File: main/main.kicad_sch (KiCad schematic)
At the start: 37 parts, among them J3 USB_C_Receptacle_USB2.0_16P, J4 SM03B-SRSS-TB, Q1 DMG1012T-7, SW1 PTS810 SJK 250 SMTR LFS, U2 IC_ESPIF_ESP32-C3-MINI-1-N4, U3 W25Q32RVXHJQ TR, U5 450mA 4.2V, Y1 ECS-120-8-33-JGN-TR

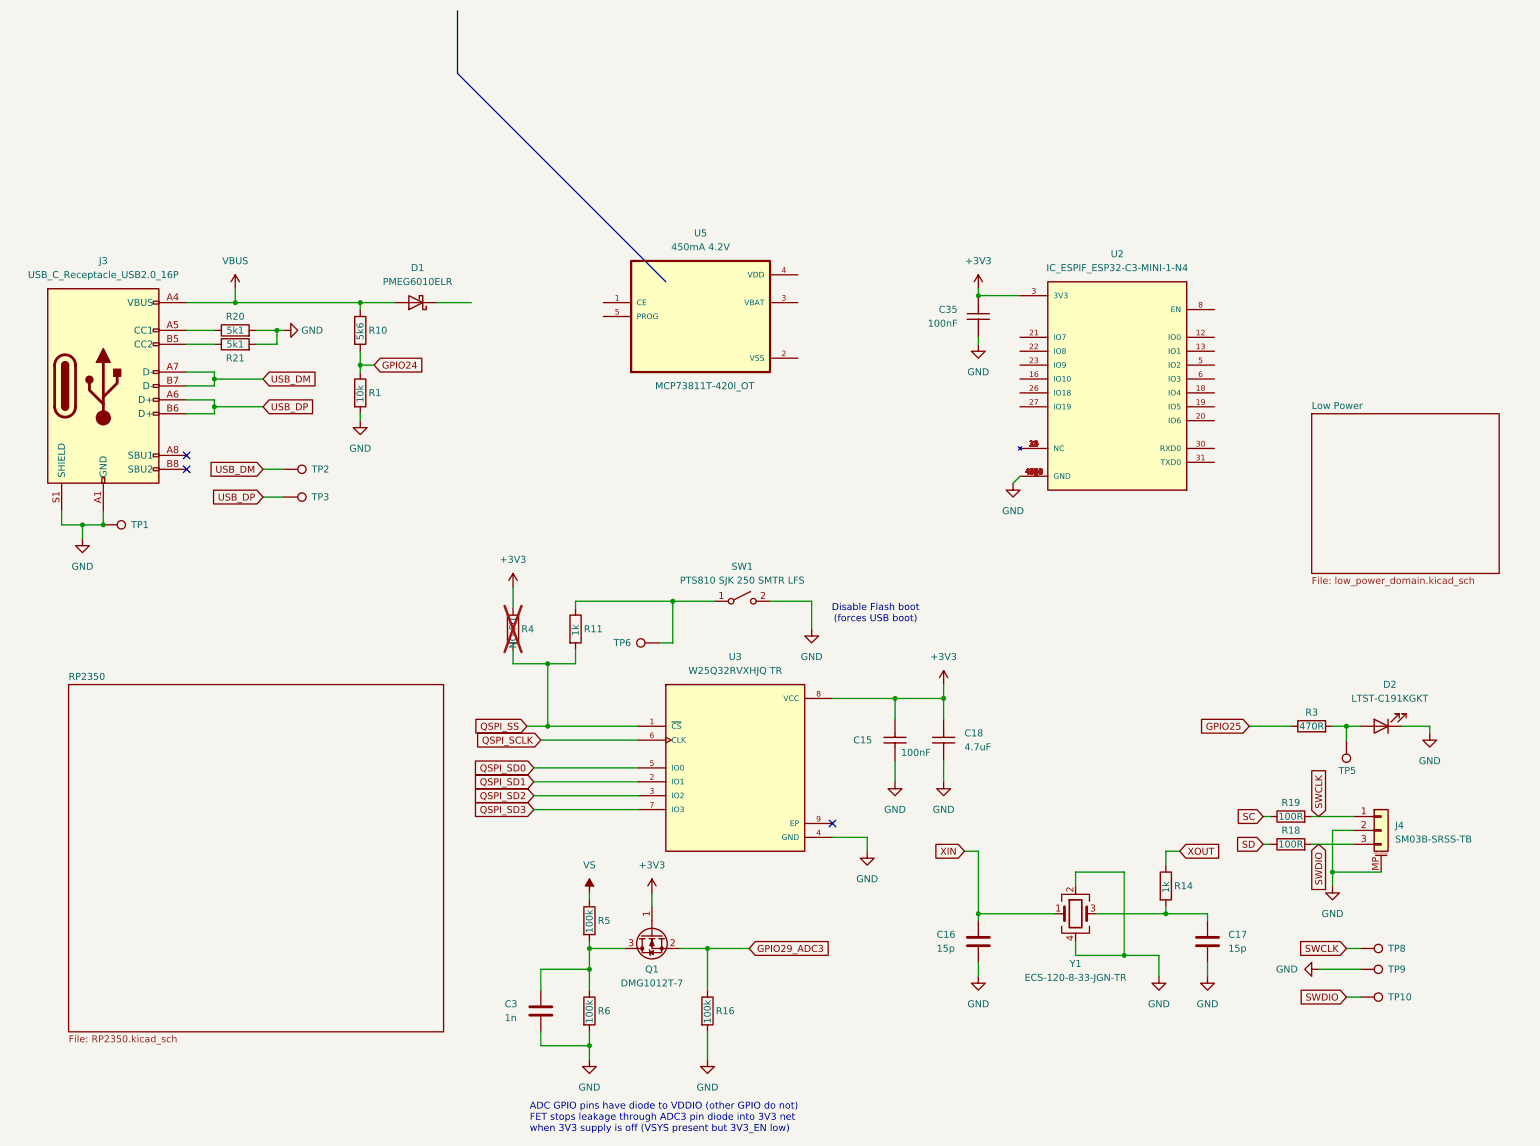
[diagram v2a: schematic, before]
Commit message: added leds and removed pico, changed outline
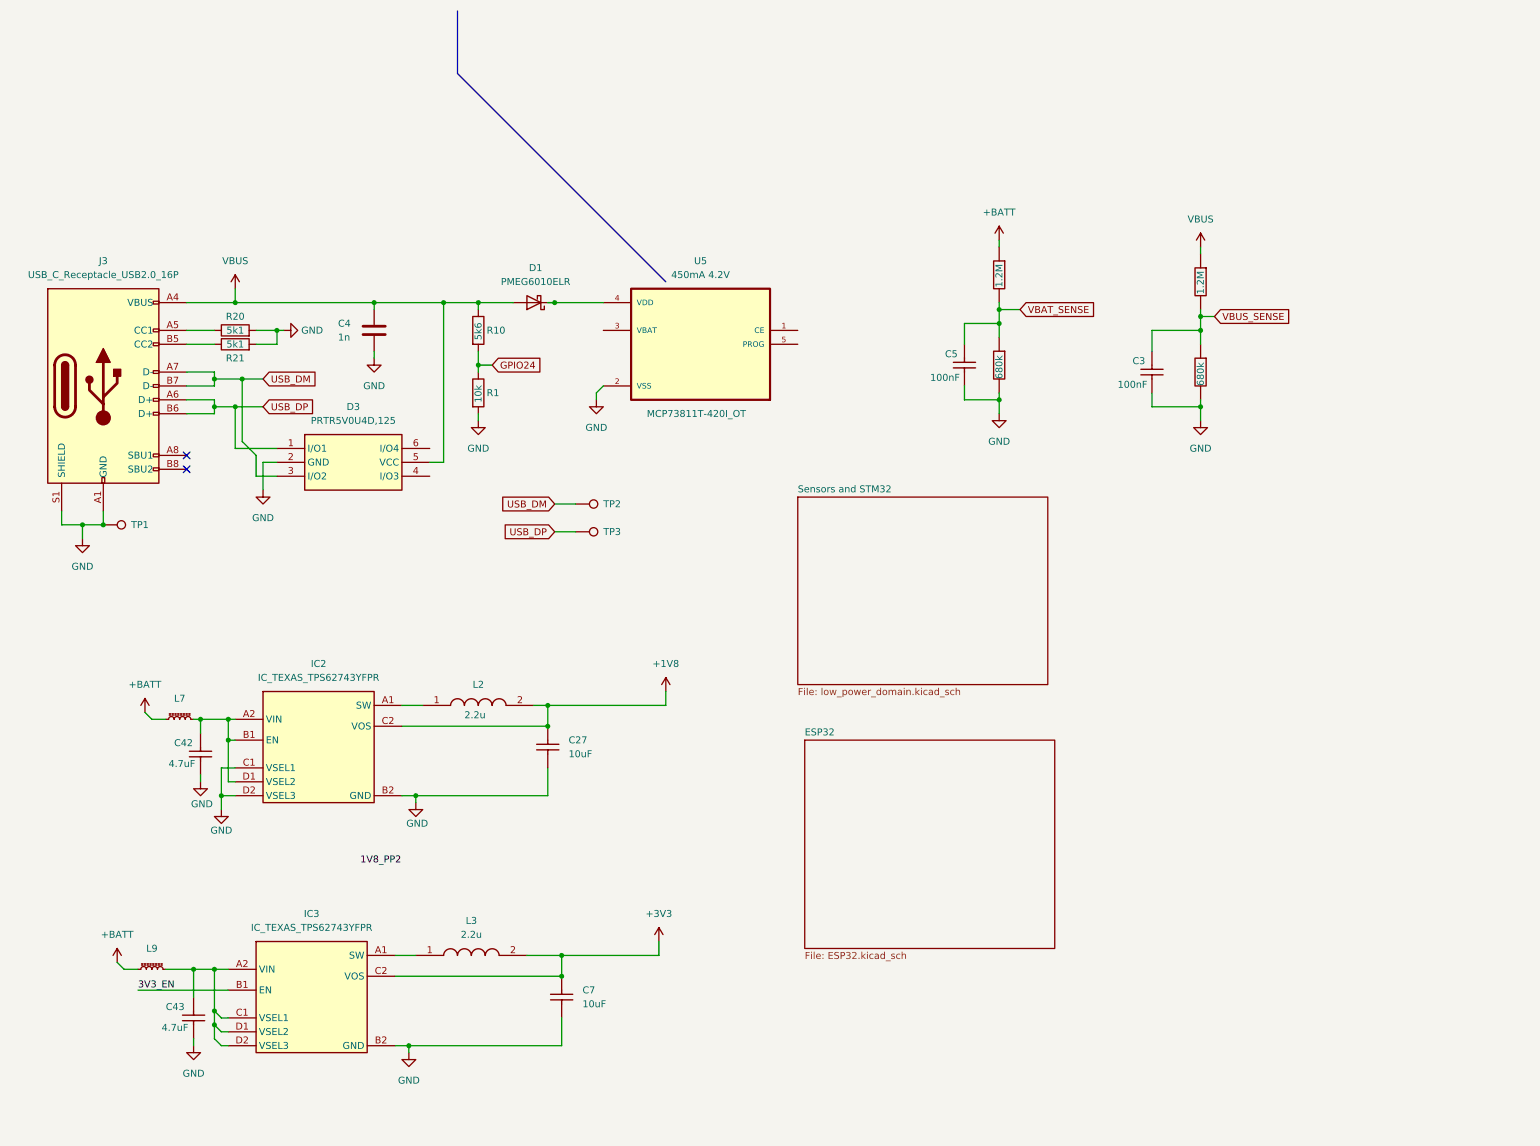
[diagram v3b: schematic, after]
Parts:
- removed C15, C35: 100NF_0201_10V_X7R, smv_footprints:C_0201_0603Metric, symbol smv_capacitors:100NF_0201_10V_X7R
- removed C16, C17: 15p, Capacitor_SMD:C_0201_0603Metric, symbol Device:C
- removed C18: 4.7UF 0402 10V X7R, smv_footprints:C_0402_1005Metric, symbol smv_capacitors:4.7UF_0402_10V_X7R
- removed D2: LTST-C191KGKT, LED_SMD:LED_0603_1608Metric, symbol Device:LED
- removed J4: SM03B-SRSS-TB, Connector_JST:JST_SH_SM03B-SRSS-TB_1x03-1MP_P1.00mm_Horizontal, symbol Connector_Generic_MountingPin:Conn_01x03_MountingPin
- removed Q1: DMG1012T-7, Package_TO_SOT_SMD:SOT-523, symbol Device:Q_NMOS_GSD
- removed R11, R14: 1k, Resistor_SMD:R_0201_0603Metric, symbol Device:R
- removed R16, R6: 100k, Resistor_SMD:R_0201_0603Metric, symbol Device:R
- removed R18, R19: 100R, Resistor_SMD:R_0201_0603Metric, symbol Device:R
- removed R3: 470R, Resistor_SMD:R_0201_0603Metric, symbol Device:R
- removed R4: NO-FIT, Resistor_SMD:R_0201_0603Metric, symbol Device:R
- removed SW1: PTS810 SJK 250 SMTR LFS, Button_Switch_SMD:SW_SPST_PTS810, symbol Switch:SW_SPST
- removed TP10, TP5, TP6, TP8, TP9: TestPoint, TestPoint:TestPoint_Pad_1.5x1.5mm, symbol Connector:TestPoint
- removed U2: IC_ESPIF_ESP32-C3-MINI-1-N4, smv_footprints:IC_ESPIF_ESP32-C3-MINI-1-N4, symbol smv_ic:IC_ESPIF_ESP32-C3-MINI-1-N4
- removed U3: W25Q32RVXHJQ TR, Package_DFN_QFN:TDFN-8-1EP_3x2mm_P0.5mm_EP1.3x1.4mm, symbol Pico 2 C:W25Q16JVUXIQ TR
- removed Y1: ECS-120-8-33-JGN-TR, Crystal:Crystal_SMD_SeikoEpson_FA238-4Pin_3.2x2.5mm, symbol Device:Crystal_GND24
- added C27, C7: 10UF_0805_16V_X7R, smv_footprints:C_0805_2012Metric, symbol smv_capacitors:10UF_0805_16V_X7R
- added C4: 1n, Capacitor_SMD:C_0201_0603Metric, symbol Device:C
- added C42, C43: 4.7UF 0402 10V X7R, smv_footprints:C_0402_1005Metric, symbol smv_capacitors:4.7UF_0402_10V_X7R
- added C5: 100NF_0201_10V_X7R, smv_footprints:C_0201_0603Metric, symbol smv_capacitors:100NF_0201_10V_X7R
- added D3: PRTR5V0U4D,125, SOT95P275X110-6N, symbol smv_diodes:DIOD_NEXPERIA_PRTR5V0U4D,125
- added IC2, IC3: IC_TEXAS_TPS62743YFPR, smv_footprints:BGA8C40P2X4_87X156X53, symbol smv_ic:IC_TEXAS_TPS62743YFPR
- added L2, L3: 2.2u, smv_footprints:IND_MURATA_DFE201610P-2R2M=P2, symbol smv_inductors:IND_MURATA_DFE201610P-2R2M=P2
- added L7, L9: INDC_BEAD_BLM18AG601SN1D, Inductor_SMD:L_0603_1608Metric, symbol smv_inductors:INDC_BEAD_BLM18AG601SN1D
- added R6, R9: 680K 0402, smv_footprints:R_0402_1005Metric, symbol smv_resistors:680K 0402
- added R7: 1.2M 0402, smv_footprints:R_0402_1005Metric, symbol smv_resistors:1.2M 0402
- C3: value 1n -> 100NF_0201_10V_X7R; footprint Capacitor_SMD:C_0201_0603Metric -> smv_footprints:C_0201_0603Metric; symbol Device:C -> smv_capacitors:100NF_0201_10V_X7R; Voltage (none) -> 0V; manf (none) -> Generic; manfn# (none) -> Generic; val (none) -> 100nF
- R5: value 100k -> 1.2M 0402; footprint Resistor_SMD:R_0201_0603Metric -> smv_footprints:R_0402_1005Metric; symbol Device:R -> smv_resistors:1.2M 0402; manf (none) -> Generic; val (none) -> 1.2M
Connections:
- net VS is gone; now on net VBUS_SENSE: R5.1
- net +3V3: now also C7.1, IC3.C2 (VOS), L3.2
- net GND: now also U5.2 (VSS), C27.2, C4.2, C42.2, C43.2, C5.2, C7.2, D3.2 (GND), IC2.B2 (GND), IC2.C1 (VSEL1), IC2.D2 (VSEL3), IC3.B2 (GND), R6.1, R9.1
- net USB_DM: now also D3.3 (I/O2)
- net USB_DP: now also D3.1 (I/O1)
- net VBUS: now also R5.2, C4.1, D3.5 (VCC)
- net VBUS_SENSE: now reaches C3.1
- net VBUS_SENSE: now also R6.2; no longer R5.2
- net at D1.1 (K): now also U5.4 (VDD)
- new net: IC2.A1 (SW), L2.1
- new net: C43.1, IC3.A2 (VIN), IC3.C1 (VSEL1), IC3.D1 (VSEL2), IC3.D2 (VSEL3), L9.2
- new net: IC3.A1 (SW), L3.1
- new net: C42.1, IC2.A2 (VIN), IC2.B1 (EN), IC2.D1 (VSEL2), L7.2
- new net +1V8: C27.1, IC2.C2 (VOS), L2.2
- new net +BATT: L7.1, L9.1, R7.2
- new net 3V3_EN: IC3.B1 (EN)
- new net VBAT_SENSE: C5.1, R7.1, R9.2
- no-connect marks 3 -> 2
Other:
- sheet Low Power renamed Sensors and STM32
- removed sheet RP2350
- added sheet ESP32 (ESP32.kicad_sch)
- note removed: "ADC GPIO pins have diode to VDDIO (other GPIO do not) FET stops leakage through ADC3 pin diode into 3V3 net when 3V3 supply is off (VSYS present but 3V3_EN low)"
- note removed: "Disable Flash boot (forces USB boot)"
- moved on the sheet: D1, R1, R10, TP2, TP3, U5
